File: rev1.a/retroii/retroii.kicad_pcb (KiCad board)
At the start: 4 copper layers, 284 parts, among them CON1 SD_Card_SPI, J1 VGA, J10 BARREL_JACK, J11 Conn_02x10, J12 Peripheral Slot 0, J13 74LS74, J14 Game_IO_Socket, J15 Peripheral Slot 4, J16 Peripheral Slot 1, J17 Peripheral Slot 5, J18 Peripheral Slot 2, J19 Peripheral Slot 6, J2 Joystick 1, J20 Peripheral Slot 3, J21 Peripheral Slot 7, J22 Conn_01x09, J23 Conn_01x02, J24 Headphone, J3 Joystick 2, J4 PC Port 1, J5 PC Port 2, J6 Edge mounted connector, J7 Cassette In, J8 Cassette Out, J9 Speaker Jack, K1 PS2_KEYBOARD, K13 LM741, P1 PROP_PLUG, P2 PROP_PLUG, Q4 MPSA13, Q5 2N3904, SW1 SW_PUSH_SAFE, SW2 SPST2, SW3 SAVE, SW4 LOAD, SW5 SW_PUSH_SAFE, SW6 RESET, SW7 MISC1, SW8 MISC2, U1 74LS00, U10 74LS08, U11 LM2576-12, U12 LM2576-5, U13 LM2576-12, U14 LM2576-3.3, U15 LM2576-5, U16 Prop_P8X32A, U17 24LC256_EEPROM, U18 74LS04, U3 74LS11, U4 Prop_P8X32A, U5 24LC256_EEPROM, U6 AT28C256_EEPROM, U8 IDT7008_Dual_Port_RAM, U9 74LS32, Y1 5MHz 20pf, Y2 ECS-2100X-1MHZ, Y3 5MHz 20pf

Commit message: address decoding layout
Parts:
- moved U11 129.9 mm to (232.0, 82.4)
- moved C19 129.9 mm to (341.3, 85.5)
- moved C20 129.9 mm to (237.3, 110.8)
- moved C21 129.9 mm to (317.4, 111.1)
- moved C23 129.9 mm to (302.4, 95.0)
- moved C24 129.9 mm to (328.3, 85.1)
- moved C25 129.9 mm to (327.1, 107.6)
- moved C26 129.9 mm to (317.4, 120.7)
- moved C27 129.9 mm to (345.7, 95.1)
- moved C28 129.9 mm to (327.1, 117.2)
- moved C29 129.9 mm to (336.9, 106.7)
- moved C30 129.9 mm to (276.2, 128.0)
- moved C33 129.9 mm to (335.9, 97.2)
- moved D1 129.9 mm to (296.9, 65.5)
- moved D2 129.9 mm to (268.9, 101.6)
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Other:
- board outline added: 362 x 215.9 mm

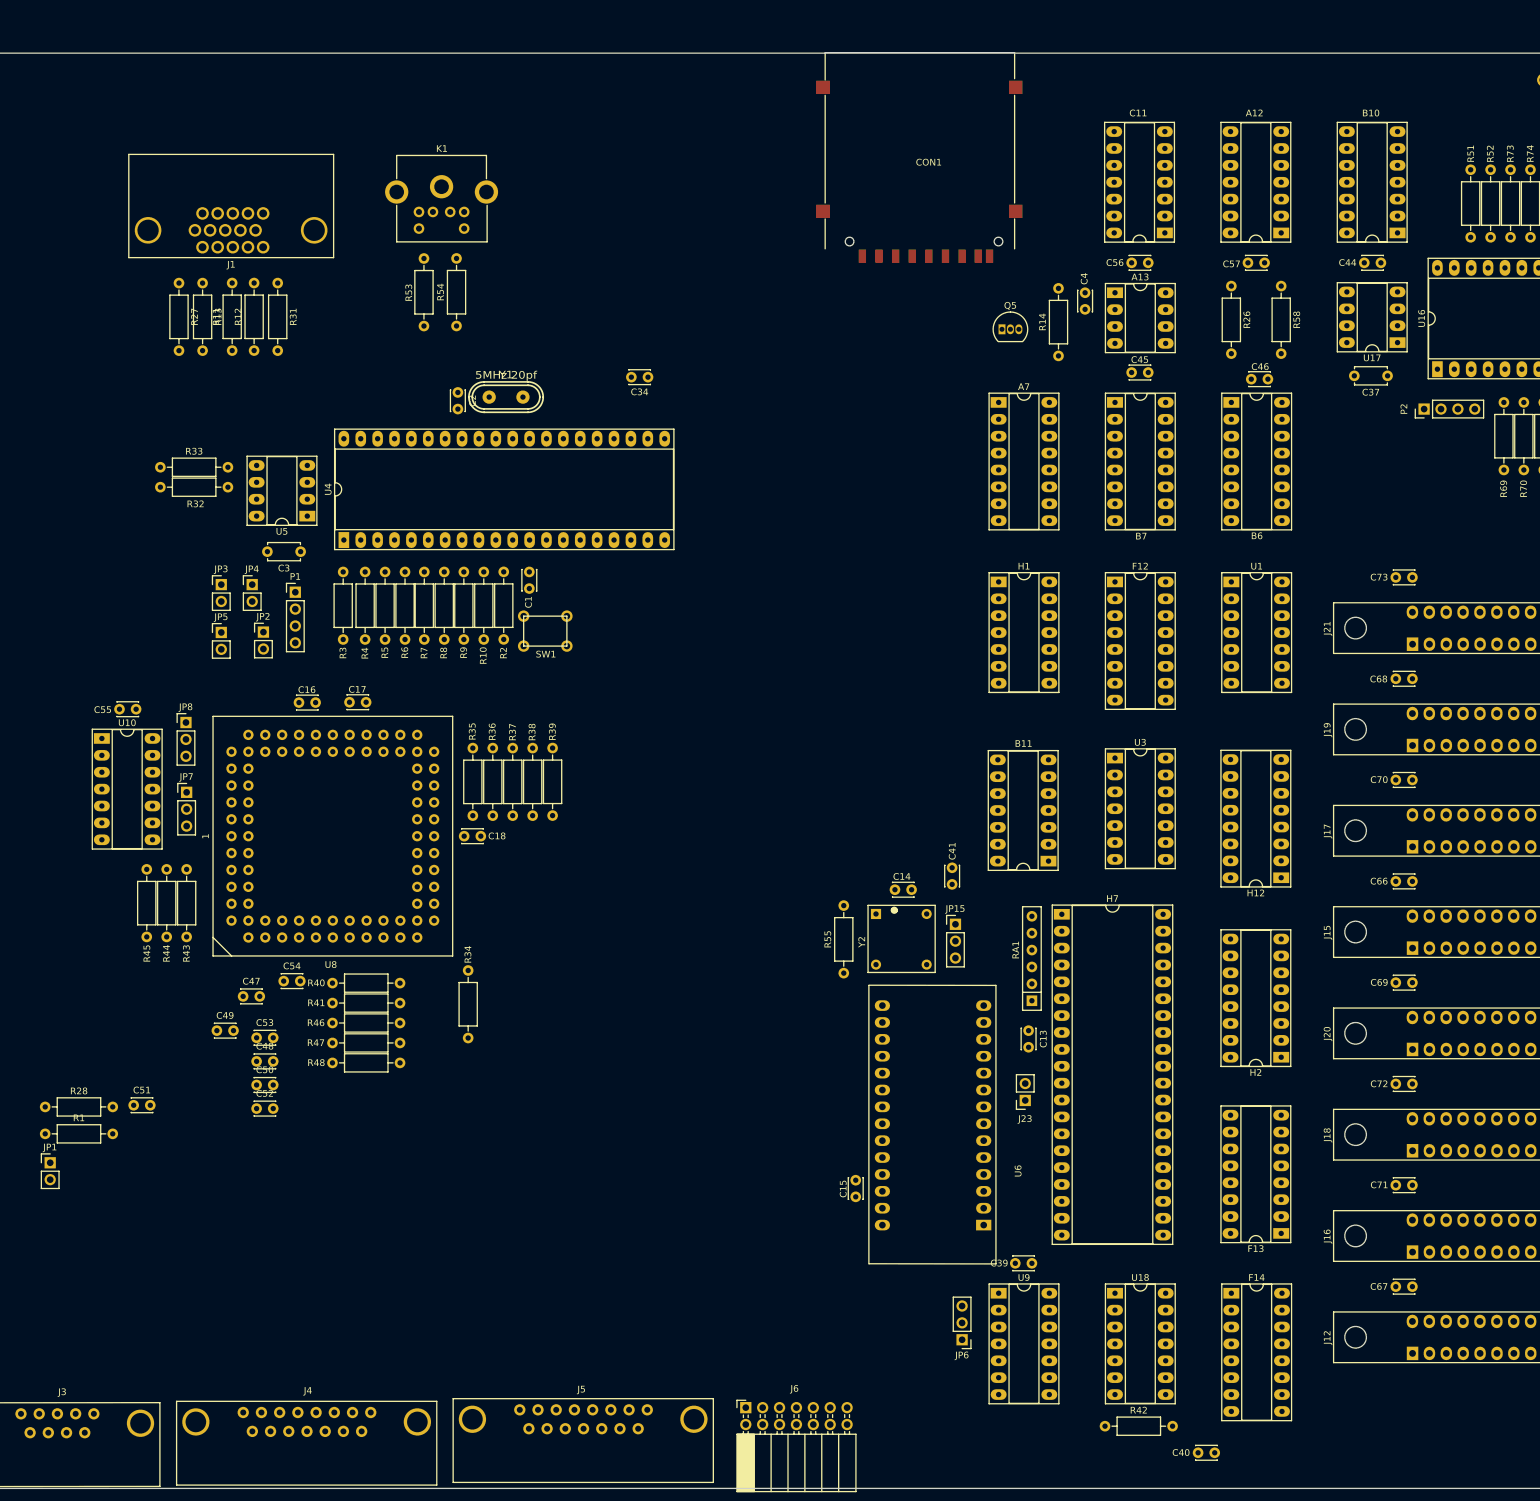
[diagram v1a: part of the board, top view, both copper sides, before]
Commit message: layout ram/video/sd/keyboard
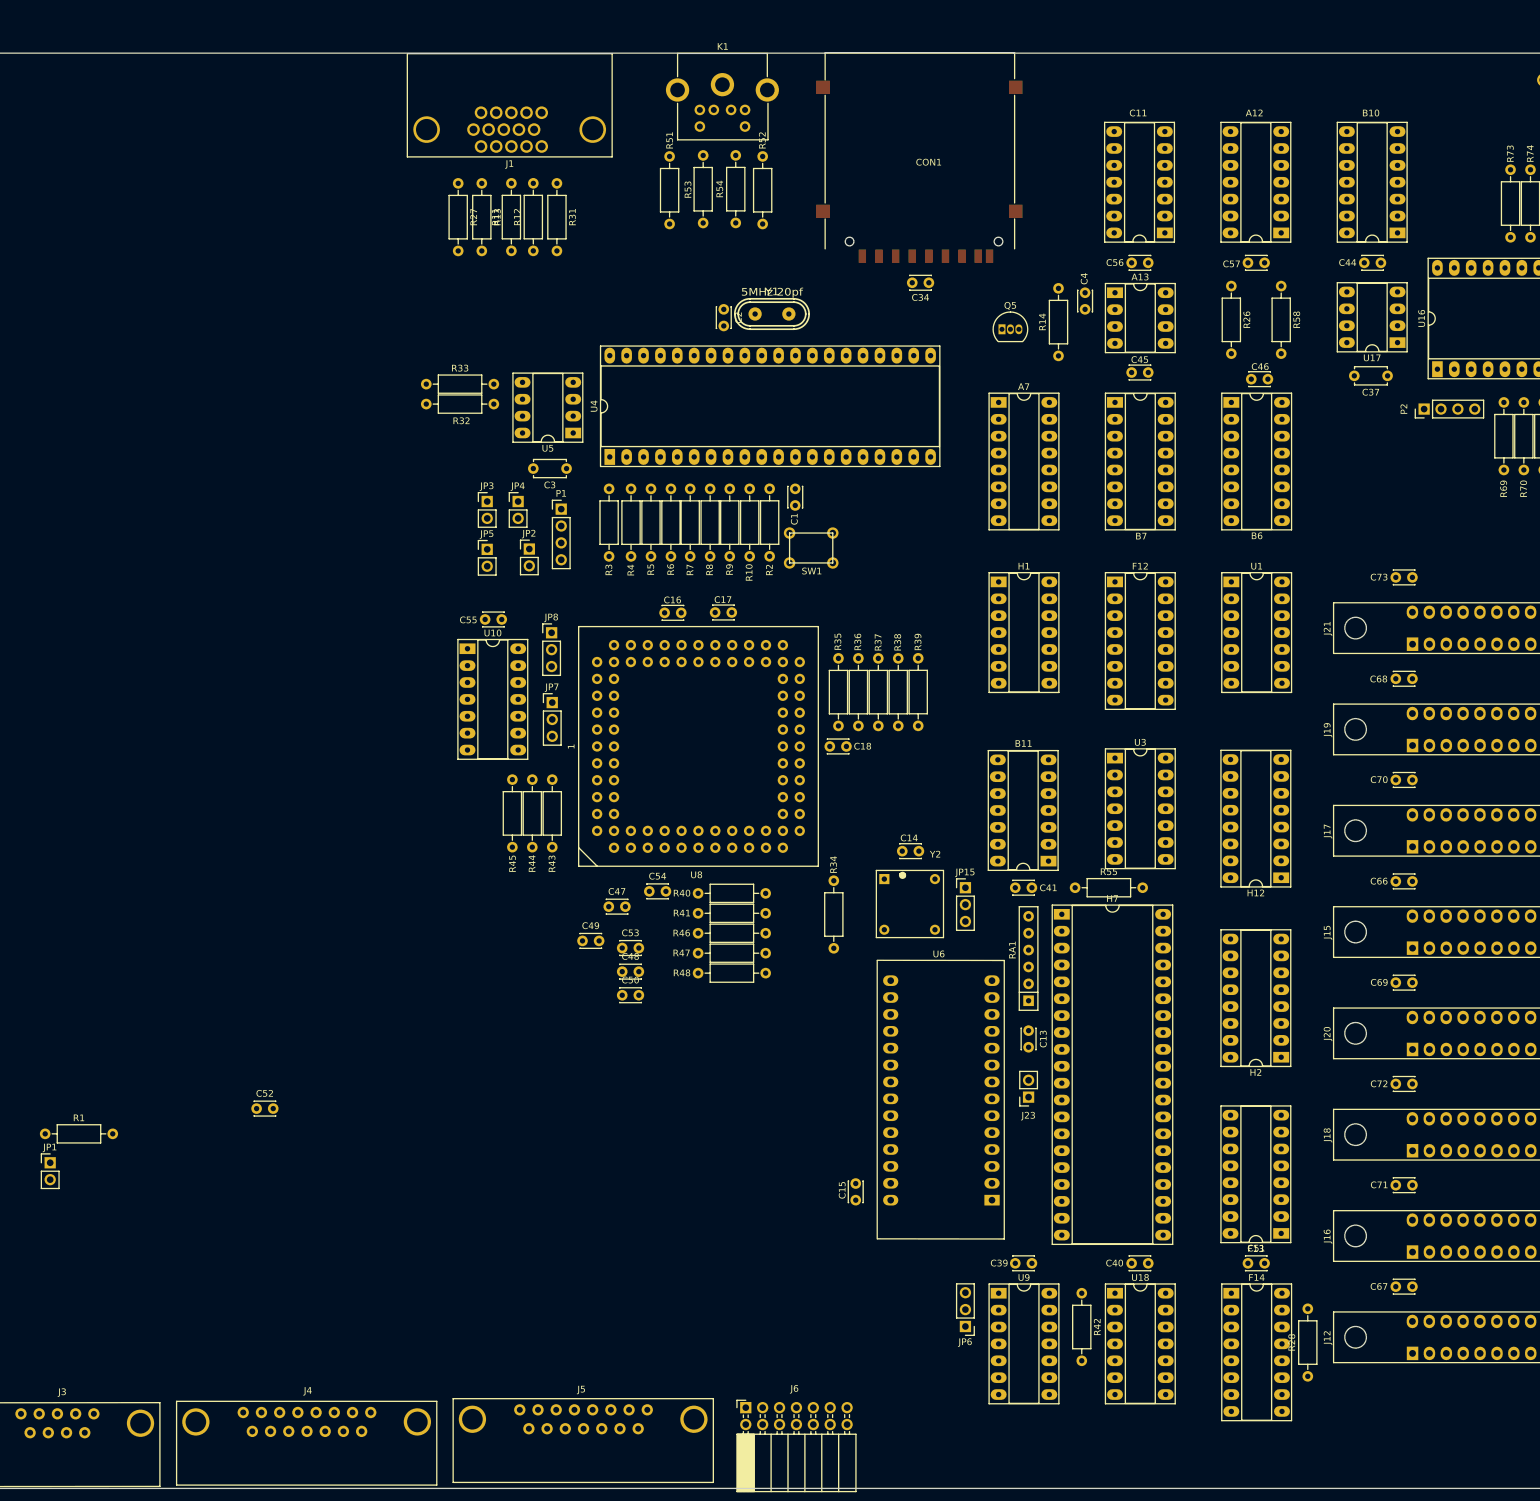
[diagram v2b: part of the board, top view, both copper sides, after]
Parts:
- moved R28 194.2 mm to (467.5, 349.0), turned to 90 degrees
- moved C51 169.3 mm to (458.5, 332.0)
- moved R51 120.5 mm to (371.5, 165.5)
- moved R52 109.5 mm to (385.5, 165.5)
- moved C16 56.6 mm to (370.8, 234.2)
- moved C17 56.6 mm to (378.4, 234.1)
- moved C18 56.6 mm to (395.6, 254.2)
- moved C47 56.6 mm to (362.4, 278.4)
- moved C48 56.6 mm to (364.4, 288.1)
- moved C49 56.6 mm to (358.4, 283.5)
- moved C50 56.6 mm to (364.4, 291.7)
- moved C53 56.6 mm to (364.4, 284.6)
- moved C54 56.6 mm to (368.4, 276.1)
- moved C55 56.6 mm to (346.2, 235.2)
- moved JP8 56.6 mm to (353.8, 237.2)
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
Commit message: more layout
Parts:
- moved C18 90.2 mm to (306.1, 265.2)
- moved C14 73.6 mm to (405.0, 343.5), turned to 0 degrees
- moved C48 67.8 mm to (303.1, 259.1), turned to 270 degrees
- moved R34 66.1 mm to (451.0, 311.5), turned to 90 degrees
- moved JP15 63.3 mm to (397.5, 336.0), turned to 180 degrees
- moved C53 63.1 mm to (306.7, 259.1), turned to 270 degrees
- moved C50 61.5 mm to (304.9, 275.9), turned to 90 degrees
- moved B11 61.2 mm to (395.5, 323.0)
- moved C41 60.5 mm to (391.0, 326.5)
- moved C15 60.4 mm to (451.0, 288.5), turned to 90 degrees
- moved C49 59.0 mm to (307.8, 253.2), turned to 270 degrees
- moved Y2 57.5 mm to (406.5, 335.5), turned to 90 degrees
- moved C54 54.8 mm to (315.2, 263.2), turned to 270 degrees
- moved R55 53.9 mm to (420.5, 328.0)
- moved C47 53.8 mm to (312.9, 257.1), turned to 270 degrees
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
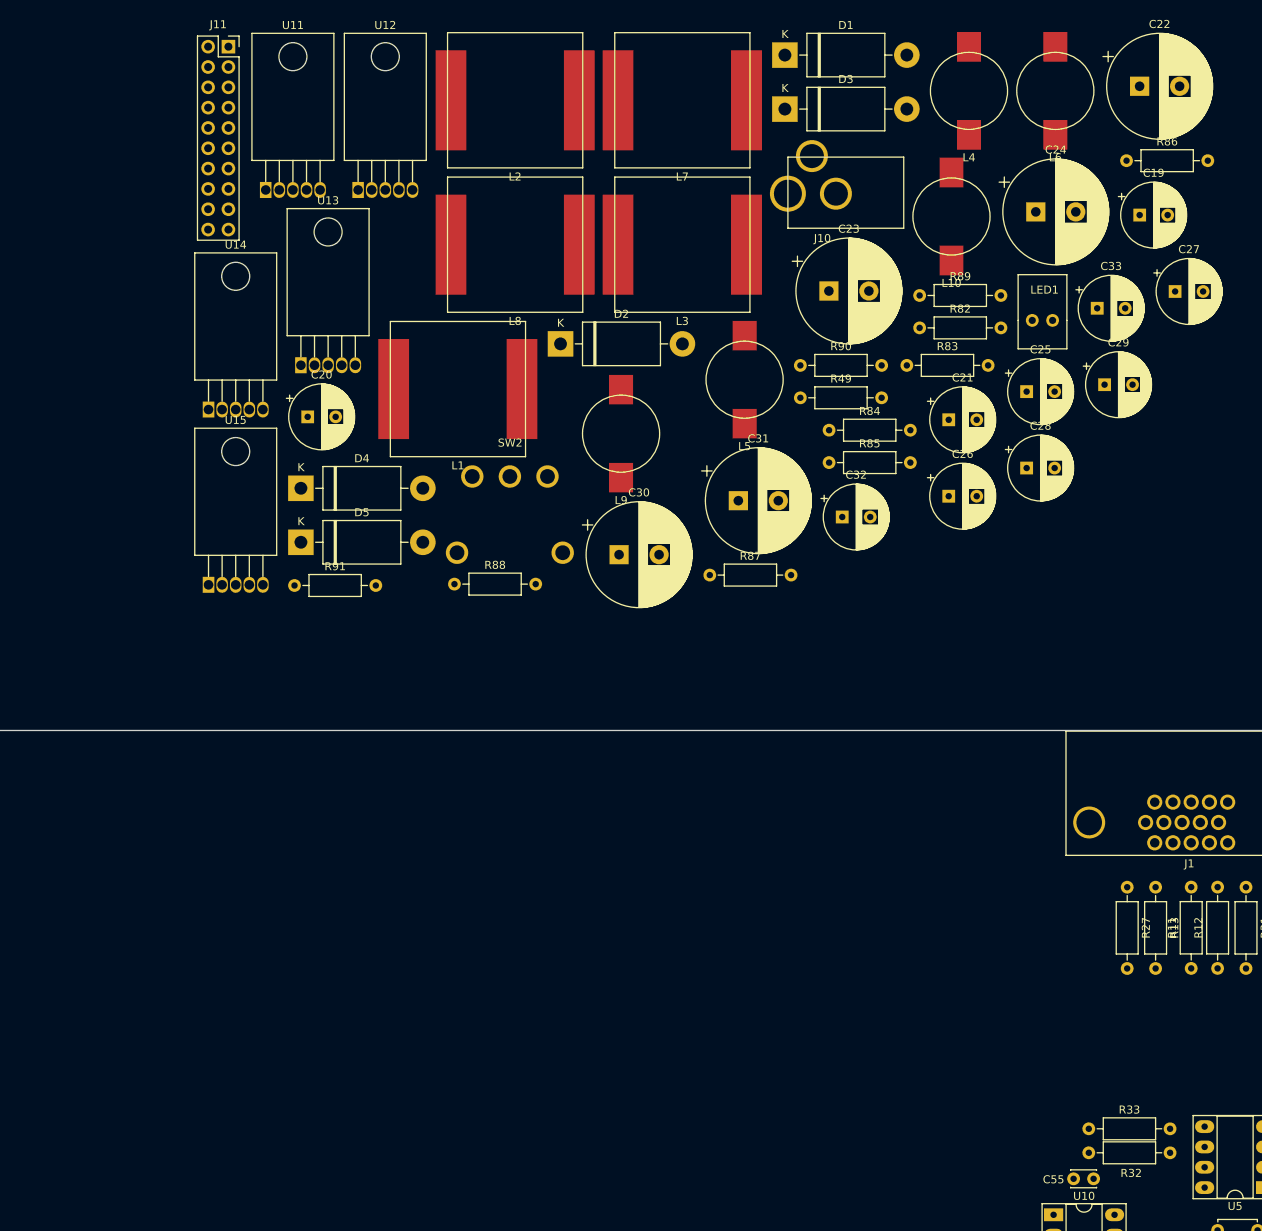
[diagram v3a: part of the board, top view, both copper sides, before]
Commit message: beginning power supply layout
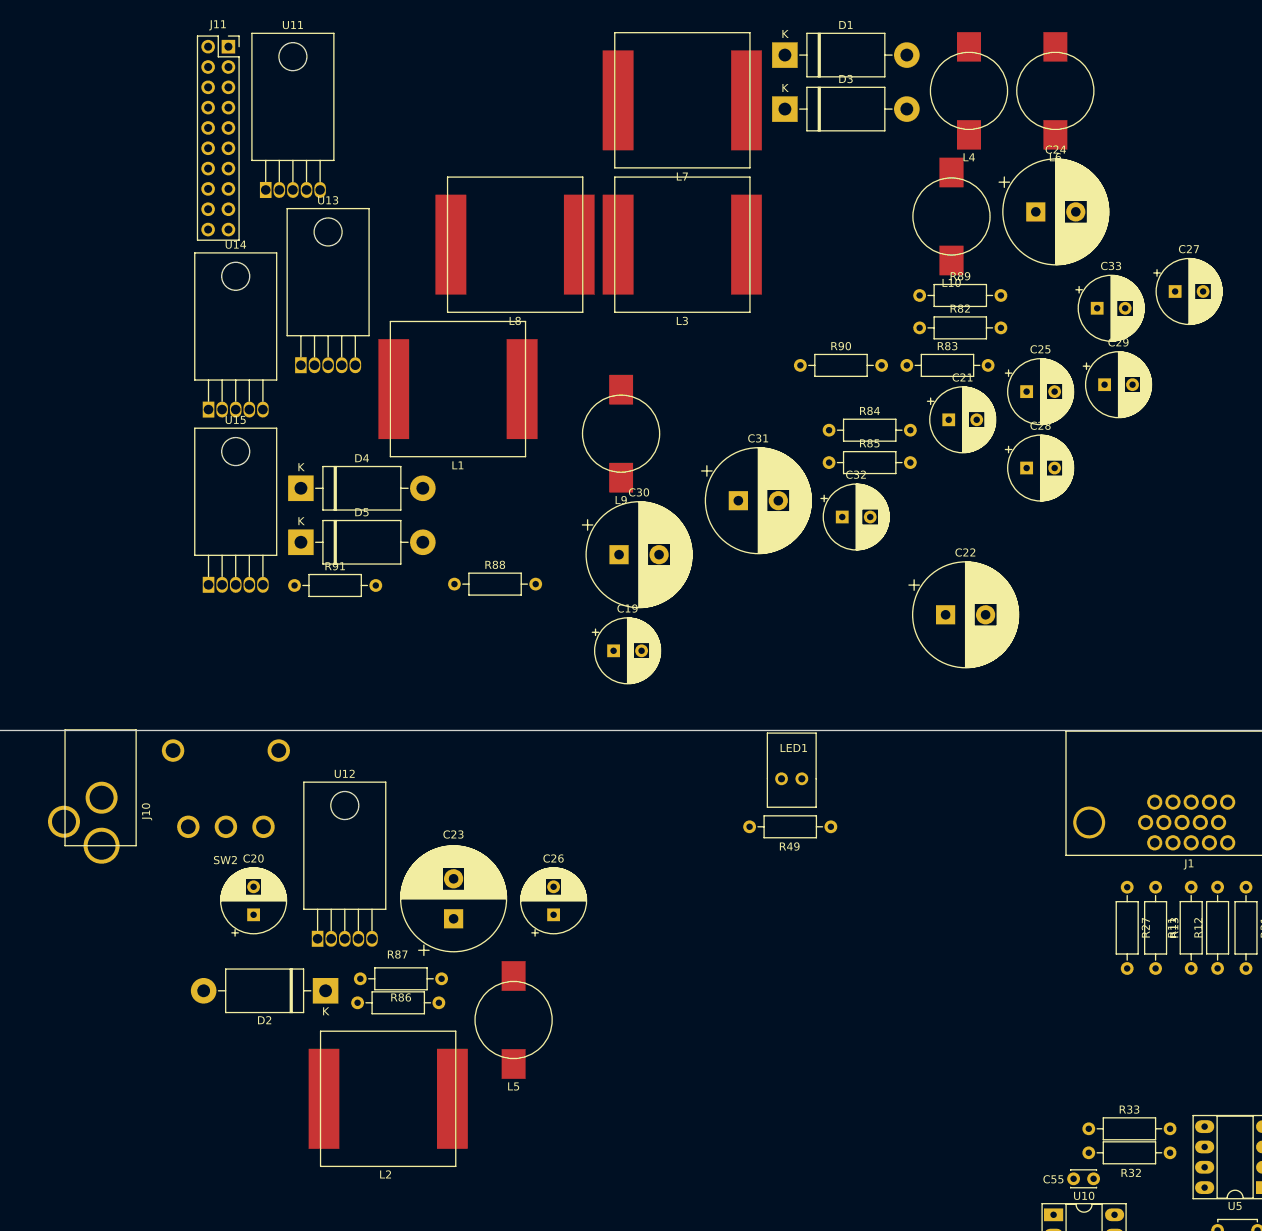
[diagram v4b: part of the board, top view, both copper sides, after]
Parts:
- moved R86 133.4 mm to (254.0, 181.0), turned to 180 degrees
- moved L2 124.8 mm to (255.0, 196.0), turned to 180 degrees
- moved J10 119.1 mm to (211.5, 157.0), turned to 90 degrees
- moved U12 93.7 mm to (238.5, 176.0)
- moved C23 91.4 mm to (255.5, 173.5), turned to 90 degrees
- moved D2 86.0 mm to (239.5, 182.5), turned to 180 degrees
- moved C19 85.4 mm to (275.5, 140.0)
- moved L5 85.1 mm to (263.0, 181.0)
- moved C26 72.0 mm to (268.0, 173.0), turned to 90 degrees
- moved C22 70.4 mm to (317.0, 135.5)
- moved R87 69.3 mm to (243.5, 184.0)
- moved LED1 65.3 mm to (296.5, 156.0)
- moved C20 62.6 mm to (230.5, 173.0), turned to 90 degrees
- moved SW2 56.4 mm to (227.0, 162.0), turned to 180 degrees
- moved R49 54.0 mm to (292.5, 162.0)

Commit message: added more in/out caps for psu. finished initial layout of psu.
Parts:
- added C80: DNP, retroii_footprints:C_Disc_D3.0mm_W2.0mm_P2.50mm, F.Cu at (211.5, 192.2)
- added C81: DNP, retroii_footprints:C_Disc_D3.0mm_W2.0mm_P2.50mm, F.Cu at (272.5, 227.0)
- added C82: DNP, retroii_footprints:C_Disc_D3.0mm_W2.0mm_P2.50mm, F.Cu at (271.5, 279.8)
- added C83: DNP, retroii_footprints:C_Disc_D3.0mm_W2.0mm_P2.50mm, F.Cu at (251.5, 186.0)
- added C84: DNP, retroii_footprints:C_Disc_D3.0mm_W2.0mm_P2.50mm, F.Cu at (312.5, 223.2)
- added C85: DNP, retroii_footprints:C_Disc_D3.0mm_W2.0mm_P2.50mm, F.Cu at (311.5, 276.0)
- added C86: DNP, retroii_footprints:C_Disc_D3.0mm_W2.0mm_P2.50mm, F.Cu at (269.8, 171.5)
- added C87: DNP, retroii_footprints:C_Disc_D3.0mm_W2.0mm_P2.50mm, F.Cu at (211.8, 248.5)
- added C88: DNP, retroii_footprints:C_Disc_D3.0mm_W2.0mm_P2.50mm, F.Cu at (309.8, 167.8)
- added C89: DNP, retroii_footprints:C_Disc_D3.0mm_W2.0mm_P2.50mm, F.Cu at (251.8, 244.8)
- added R92: 3.3K, retroii_footprints:R_Axial_DIN0207_L6.3mm_D2.5mm_P10.16mm_Horizontal, F.Cu at (430.5, 324.0)
- R55: value 0 -> DNP
- moved L6 222.0 mm to (300.0, 284.8)
- moved D3 214.9 mm to (276.5, 286.2), turned to 180 degrees
- moved L3 211.1 mm to (292.0, 299.8), turned to 180 degrees
- moved C24 195.4 mm to (292.5, 277.2), turned to 90 degrees
- moved C29 191.1 mm to (205.2, 245.2), turned to 90 degrees
- moved L10 189.5 mm to (240.2, 253.5)
- moved R82 186.5 mm to (291.0, 284.8), turned to 180 degrees
- moved R83 186.1 mm to (280.8, 287.8)
- moved C27 185.9 mm to (305.0, 276.5), turned to 90 degrees
- moved R89 185.7 mm to (221.0, 256.5)
- moved L8 180.8 mm to (232.2, 268.5), turned to 180 degrees
- moved U13 179.7 mm to (275.5, 279.8)
- moved C33 173.6 mm to (245.2, 245.2), turned to 90 degrees
- moved C21 173.5 mm to (265.0, 276.5), turned to 90 degrees
- moved J11 166.3 mm to (250.2, 229.2), turned to 180 degrees
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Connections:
- H7 pad 2: /CPU_RAM_ROM/RDY -> Net-(H7-Pad2)

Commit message: started audio/cassette in/out layout
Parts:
- moved H14 242.2 mm to (297.2, 316.0)
- moved J13 161.2 mm to (240.2, 307.0)
- moved R57 154.8 mm to (259.2, 317.2), turned to 90 degrees
- moved R29 142.4 mm to (253.5, 343.0), turned to 90 degrees
- moved LS1 129.7 mm to (223.5, 306.0), turned to 90 degrees
- moved K13 125.7 mm to (240.0, 334.2)
- moved R67 123.7 mm to (256.2, 317.2), turned to 90 degrees
- moved R56 123.6 mm to (253.2, 317.2), turned to 90 degrees
- moved R30 120.6 mm to (232.2, 343.2), turned to 90 degrees
- moved R18 118.8 mm to (223.0, 324.5), turned to 180 degrees
- moved C10 101.5 mm to (226.2, 339.8), turned to 90 degrees
- moved R19 92.0 mm to (223.0, 321.5), turned to 180 degrees
- moved JP18 77.7 mm to (219.0, 314.0), turned to 90 degrees
- moved J11 72.3 mm to (321.8, 239.8), turned to 0 degrees
- moved C21 69.0 mm to (204.5, 243.2)
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
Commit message: audio cassette in/out layout
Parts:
- moved CR1 285.9 mm to (365.1, 321.9), turned to 90 degrees
- moved Q4 266.1 mm to (347.5, 336.8), turned to 90 degrees
- moved J14 241.8 mm to (307.2, 326.0), turned to 180 degrees
- moved H132 235.3 mm to (339.8, 323.2), turned to 180 degrees
- moved R24 228.2 mm to (361.0, 323.8), turned to 90 degrees
- moved C38 225.9 mm to (361.0, 307.8), turned to 270 degrees
- moved R1 222.3 mm to (166.2, 183.8)
- moved C18 220.7 mm to (144.6, 184.0)
- moved C48 220.7 mm to (141.6, 177.9)
- moved C49 220.7 mm to (146.2, 171.9)
- moved C50 220.7 mm to (143.4, 194.6)
- moved C53 220.7 mm to (145.2, 177.9)
- moved C54 220.7 mm to (153.7, 181.9)
- moved C47 220.7 mm to (151.4, 175.8)
- moved JP1 217.5 mm to (173.1, 188.1)
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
